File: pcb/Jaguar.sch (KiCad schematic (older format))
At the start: 52 parts

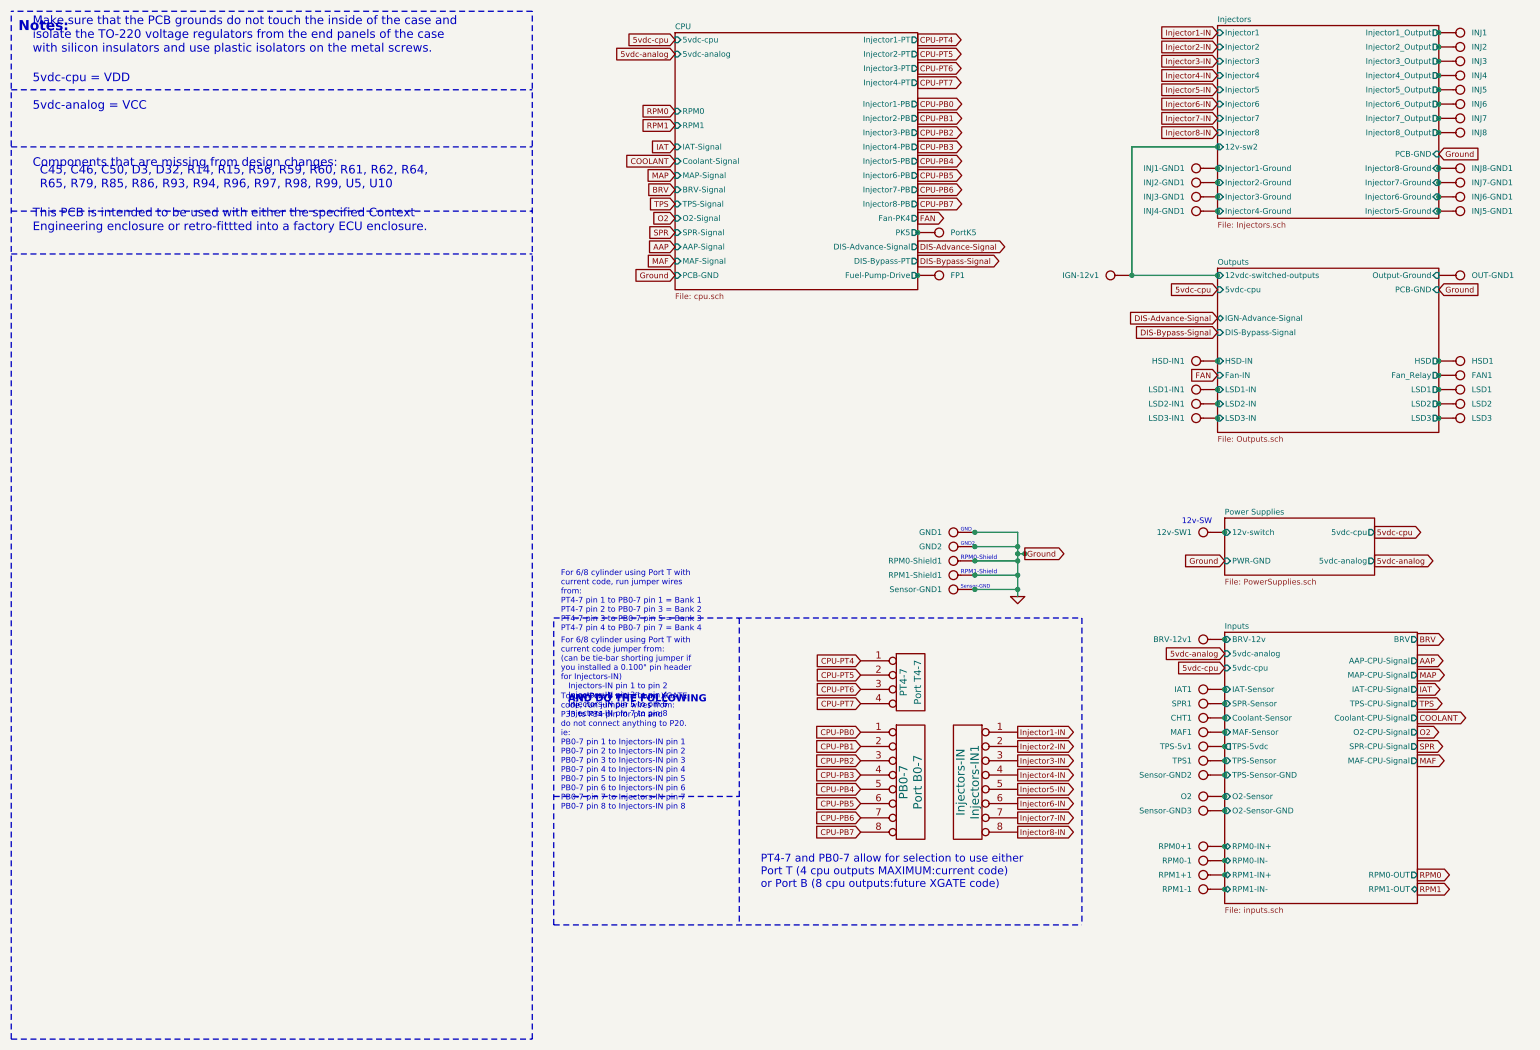
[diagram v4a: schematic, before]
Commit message: Corrected LED setup on ignitor outputs to go to ground, added diode to HSD output LED circuit, changed label called FAN to LSD2, added jumper to select using PK4 to LSD2 input, added jumper to select CPU Fuel Pump output port A7 to go to HSD or LSD4.
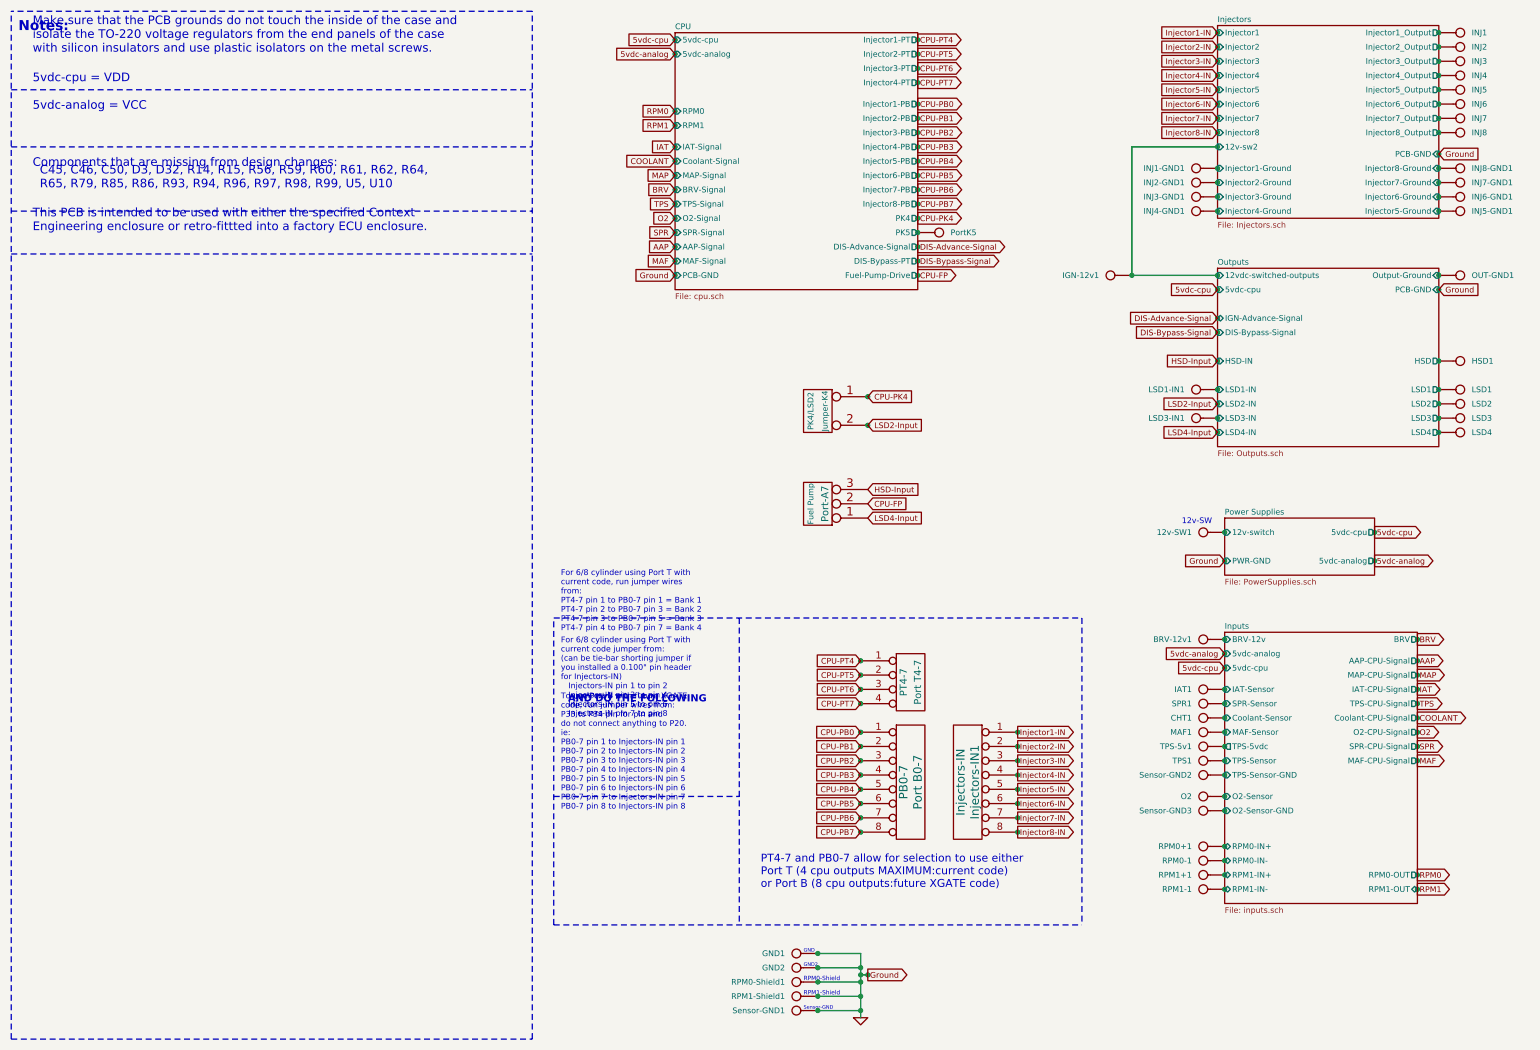
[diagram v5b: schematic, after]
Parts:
- removed FP1: FP, symbol CONN_1
- removed HSD-IN1: HSD-IN, symbol CONN_1
- removed LSD2-IN1: LSD2-IN, symbol CONN_1
- added Jumper-K4: PK4/LSD2, symbol CONN_2
- added Port-A7: Fuel Pump, symbol CONN_3
- LSD4: renamed from FAN1; value FAN -> LSD4
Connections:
- net Outputs/Fan_Relay renamed Outputs/LSD4
- new net CPU-FP: Port-A7.2 (PM)
- new net CPU-PK4: Jumper-K4.1 (P1)
- new net HSD-Input: Port-A7.3 (P3)
- new net LSD2-Input: Jumper-K4.2 (PM)
- new net LSD4-Input: Port-A7.1 (P1)
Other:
- moved on the sheet: GND1, GND2, LSD4, RPM0-Shield1, RPM1-Shield1, Sensor-GND1

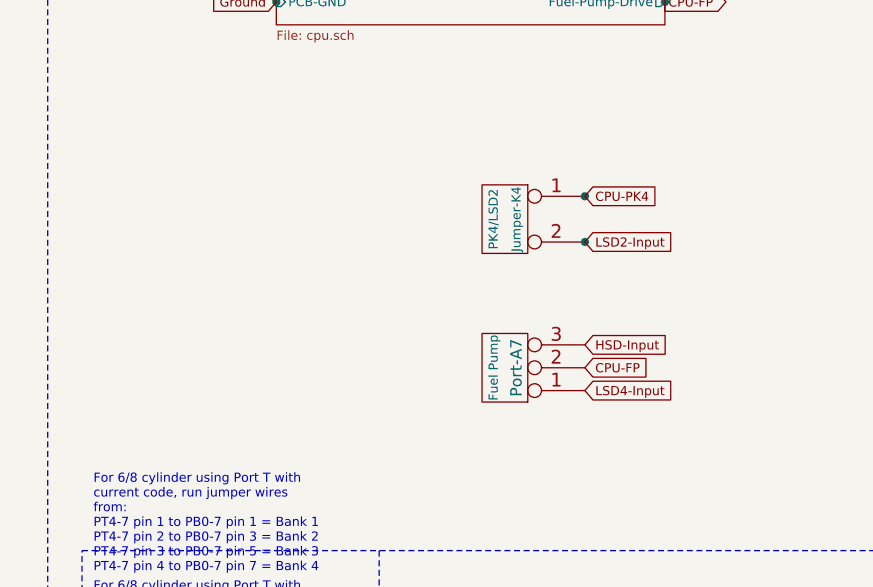
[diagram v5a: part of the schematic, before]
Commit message: Added notes about the usage of the two jumpers that were added for port K4 LSD2 and Port A7 LSD4 or HSD usage.
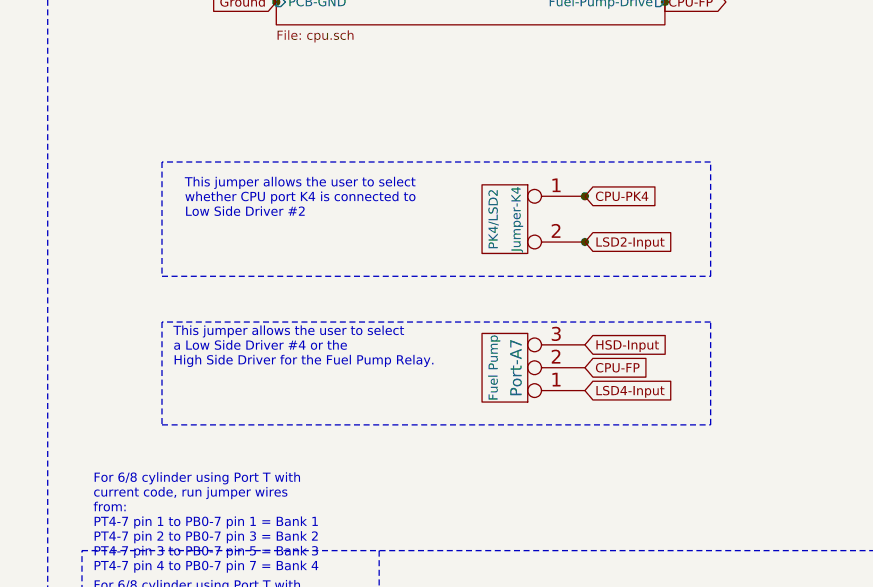
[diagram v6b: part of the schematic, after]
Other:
- note added: "This jumper allows the user to select\na Low Side Driver #4 or the\nHigh Side Driver for the Fuel Pump Relay."
- note added: "This jumper allows the user to select\nwhether CPU port K4 is connected to\nLow Side Driver #2"
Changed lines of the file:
@@
 Text GLabel 6550 3900 2    40   Input ~ 0
 HSD-Input
+Text Notes 4750 4000 0    40   ~ 0
+This jumper allows the user to select\na Low Side Driver #4 or the\nHigh Side Driver for the Fuel Pump Relay.
+Text Notes 4800 3350 0    40   ~ 0
+This jumper allows the user to select\nwhether CPU port K4 is connected to\nLow Side Driver #2
+Wire Notes Line
+	4700 3100 4700 3600
+Wire Notes Line
+	4700 3600 7100 3600
+Wire Notes Line
+	7100 3600 7100 3100
+Wire Notes Line
+	7100 3100 4700 3100
+Wire Notes Line
+	4700 3800 4700 4250
+Wire Notes Line
+	4700 4250 7100 4250
+Wire Notes Line
+	7100 4250 7100 3800
+Wire Notes Line
+	7100 3800 4700 3800
 $EndSCHEMATC
